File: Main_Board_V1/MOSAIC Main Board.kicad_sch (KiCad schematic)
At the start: 82 parts, among them J1 CONN E, J10 Right Angle Qwiic Connector, J11 Vertical Qwiic Connector, J12 CONN E, J13 CONN E, J14 35RAPC4BH3 CONN 3.5MM, J2 CONN E, J3 CONN E, J4 CONN HEADER VERT 10POS 1.27MM, J5 USB TYPE C R/A SMT 16PIN, J9 BATT JST-2-SMD, Q1 MOSFET P-CH 30V 3.1A SOT23-3, U1 IC SWITCH SP3T X 2 750mOhm TD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, U2 TVS DIODE 3.3VWM 6VC SOT26, U3 MCP73831 IC BATT CNTL, U4 IC REG LINEAR 3.3V 1A 8UDFN, U5 AP7347DQ-33W5-7K-3.3V

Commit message: started JLCPCB setup
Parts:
- J1, J12, J13, J2, J3: FT Rotation Offset (none) -> 180
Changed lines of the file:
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@@
 			)
 		)
+		(property "FT Rotation Offset" "180"
+			(at 154.178 216.408 0)
+			(effects
+				(font
+					(size 1.27 1.27)
+				)
+				(hide yes)
+			)
+		)
 		(pin "19"
 		)
@@
 			)
 		)
+		(property "FT Rotation Offset" "180"
+			(at 301.244 210.693 0)
+			(effects
+				(font
+					(size 1.27 1.27)
+				)
+				(hide yes)
+			)
+		)
 		(pin "18"
 		)
@@
 			)
 		)
+		(property "FT Rotation Offset" "180"
+			(at 62.738 216.408 0)
+			(effects
+				(font
+					(size 1.27 1.27)
+				)
+				(hide yes)
+			)
+		)
 		(pin "1"
 		)
@@
 			)
 		)
+		(property "FT Rotation Offset" "180"
+			(at 234.823 210.439 0)
+			(effects
+				(font
+					(size 1.27 1.27)
+				)
+				(hide yes)
+			)
+		)
 		(pin "18"
 		)
@@
 			(at 93.218 97.028 0)
 			(effects
+				(font
+					(size 1.27 1.27)
+				)
+				(hide yes)
+			)
+		)
+		(property "FT Rotation Offset" "180"
+			(at 93.218 97.028 0)
+			(effects

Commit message: Finished JLCPCB setup
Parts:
- C3: JLCPCB Part # C18212337 -> C20617880
- D1, D2, D3, D4, D5, S1, S2, S3, U2: FT Rotation Offset (none) -> 180
- J10: JLCPCB Part # C145956 -> C7527619
- Q1, U1, U5: FT Rotation Offset (none) -> -90
- renumbered SWDIO2 to SWDIO1
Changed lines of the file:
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@@
 			)
 		)
+		(property "FT Rotation Offset" "180"
+			(at 243.078 134.874 90)
+			(effects
+				(font
+					(size 1.27 1.27)
+				)
+				(hide yes)
+			)
+		)
 		(pin "A"
 		)
@@
 			)
 		)
+		(property "FT Rotation Offset" "-90"
+			(at 319.278 48.768 0)
+			(effects
+				(font
+					(size 1.27 1.27)
+				)
+				(hide yes)
+			)
+		)
 		(pin "3"
 		)
@@
 			)
 		)
+		(property "FT Rotation Offset" "-90"
+			(at 250.19 285.75 0)
+			(effects
+				(font
+					(size 1.27 1.27)
+				)
+				(hide yes)
+			)
+		)
 		(pin "2"
 		)
@@
 			)
 		)
+		(property "FT Rotation Offset" "180"
+			(at 278.638 69.088 0)
+			(effects
+				(font
+					(size 1.27 1.27)
+				)
+				(hide yes)
+			)
+		)
 		(pin "1"
 		)
@@
 			)
 		)
+		(property "FT Rotation Offset" "180"
+			(at 227.838 135.128 90)
+			(effects
+				(font
+					(size 1.27 1.27)
+				)
+				(hide yes)
+			)
+		)
 		(pin "A"
 		)
@@
 		(on_board yes)
 		(dnp no)
-		(property "Reference" "SWDIO2"
+		(property "Reference" "SWDIO1"
 			(at 276.0206 154.5376 0)
 			(effects
@@
 			(project "MOSAIC Main Board"
 				(path "/52f21295-3640-410f-ad83-534235adfded"
-					(reference "SWDIO2")
+					(reference "SWDIO1")
 					(unit 1)
 				)
@@
 			)
 		)
-		(property "Datasheet" "https://www.digikey.com/en/products/detail/kemet/C0603C104J4RAC7867/411096"
+		(property "Datasheet" "https://jlcpcb.com/api/file/downloadByFileSystemAccessId/8590922676573577216"
 			(at 352.298 69.088 0)
 			(effects
@@
 			)
 		)
-		(property "Description" "https://jlcpcb.com/partdetail/-KAF21BR71H104JT/C18212337"
+		(property "Description" "https://jlcpcb.com/partdetail/21992639-0805CG0R1C500NT/C20617880"
 			(at 352.298 69.088 0)
 			(effects
@@
 			)
 		)
-		(property "JLCPCB Part #" "C18212337"
+		(property "JLCPCB Part #" "C20617880"
 			(at 352.298 69.088 0)
 			(effects
@@
 			)
 		)
+		(property "FT Rotation Offset" "180"
+			(at 171.958 130.048 0)
+			(effects
+				(font
+					(size 1.27 1.27)
+				)
+				(hide yes)
+			)
+		)
 		(pin "3"
 		)
@@
 			)
 		)
+		(property "FT Rotation Offset" "180"
+			(at 311.658 61.468 0)
+			(effects
+				(font
+					(size 1.27 1.27)
+				)
+				(hide yes)
+			)
+		)
 		(pin "C"
 		)
@@
 			)
 		)
+		(property "FT Rotation Offset" "-90"
+			(at 423.418 132.588 0)
+			(effects
+				(font
+					(size 1.27 1.27)
+				)
+				(hide yes)
+			)
+		)
 		(pin "3"
 		)
@@
 			)
 		)
+		(property "FT Rotation Offset" "180"
+			(at 212.598 135.128 90)
+			(effects
+				(font
+					(size 1.27 1.27)
+				)
+				(hide yes)
+			)
+		)
 		(pin "A"
 		)
@@
 			)
 		)
+		(property "FT Rotation Offset" "180"
+			(at 311.658 140.208 90)
+			(effects
+				(font
+					(size 1.27 1.27)
+				)
+				(hide yes)
+			)
+		)
 		(pin "A"
 		)
@@
 			)
 		)
+		(property "FT Rotation Offset" "180"
+			(at 169.418 117.348 0)
+			(effects
+				(font
+					(size 1.27 1.27)
+				)
+				(hide yes)
+			)
+		)
 		(pin "3"
 		)
@@
 		)
 		(property "Value" "Right Angle Qwiic Connector"
-			(at 350.266 170.688 0)
+			(at 369.443 191.262 0)
 			(effects
 				(font
@@
 				)
 				(justify left top)
+				(hide yes)
 			)
 		)
@@
 			)
 		)
-		(property "Datasheet" "https://jlcpcb.com/api/file/downloadByFileSystemAccessId/8588895674171052032"
+		(property "Datasheet" "https://jlcpcb.com/api/file/downloadByFileSystemAccessId/8590907288981364736"
 			(at 374.523 185.928 0)
 			(effects
@@
 			)
 		)
-		(property "Description" "https://jlcpcb.com/partdetail/C145956"
+		(property "Description" "https://jlcpcb.com/partdetail/Lian_XinTechnology-XDWF_091004P/C7527619"
 			(at 374.523 185.928 0)
 			(effects
@@
 			)
 		)
-		(property "JLCPCB Part #" "C145956"
+		(property "JLCPCB Part #" "C7527619"
 			(at 374.523 185.928 0)
 			(effects
@@
 			(at 169.418 107.188 0)
 			(effects
+				(font
+					(size 1.27 1.27)
+				)
+				(hide yes)
+			)
+		)
+		(property "FT Rotation Offset" "180"
+			(at 169.418 107.188 0)
+			(effects

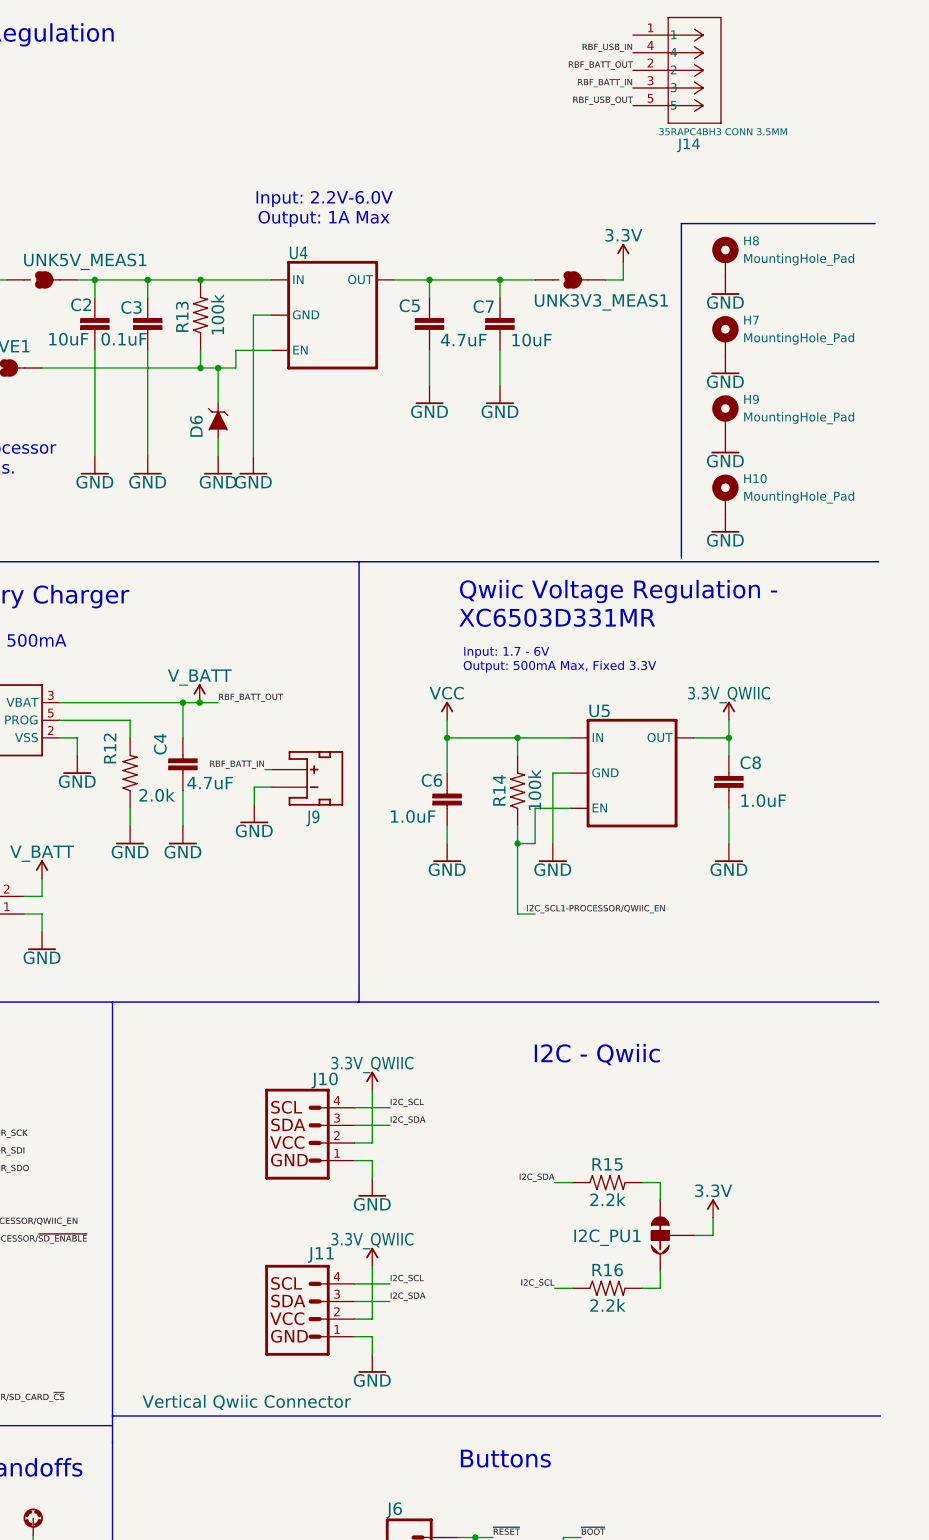
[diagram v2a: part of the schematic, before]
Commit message: added bom
Added bom for assembly after JLCPCB assembly.
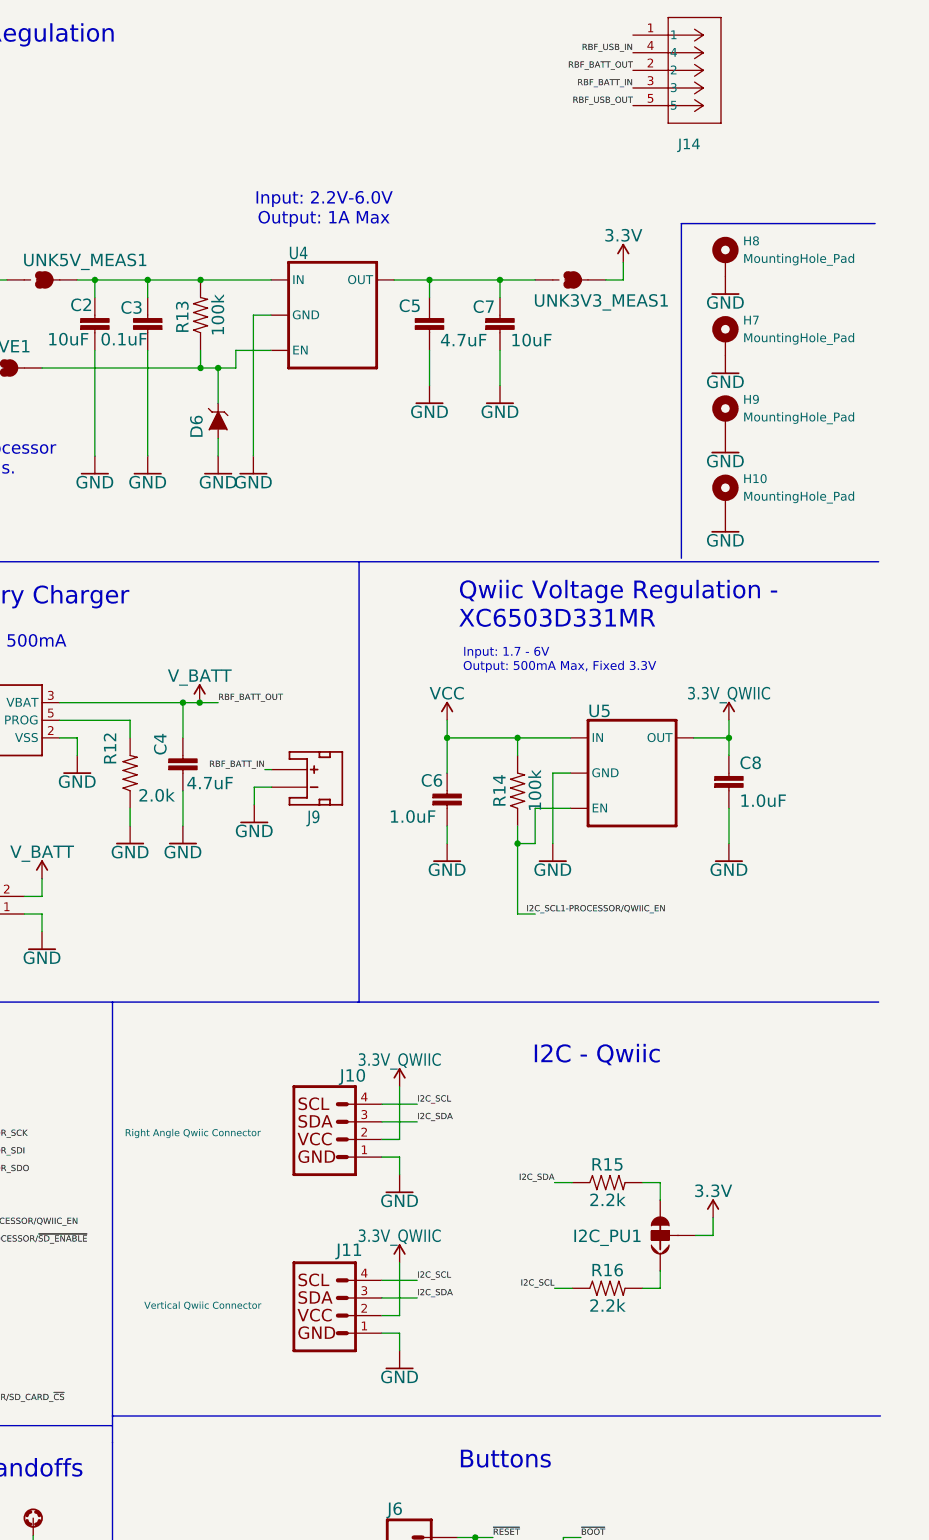
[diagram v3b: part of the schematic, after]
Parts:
- C1, C2, C3, C4, C5, C6, C7, C8, D1, D2, D3, D4, D5, D6, F1, J1, J10, J11, J12, J13, J2, J3, J5, LOGO1, LOGO2, Q1, R1, R10, R11, R12, R13, R14, R15, R16, R2, R3, R4, R5, R6, R7, R8, R9, S1, S2, S3, S4, S5, U1, U2, U3, U4, U5: now left out of the parts list
- H3: Source https://www.digikey.com/en/products/detail/w%C3%BCrth-elekt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 -> (none); now in the parts list
- J14: Source https://www.mouser.com/ProductDetail/Switchcraft/35RAPC4BH3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 -> (none); now in the parts list
- J9: value BATT JST-2-SMD -> CONN_JST_BATT; now in the parts list
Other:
- moved on the sheet: J10, J11

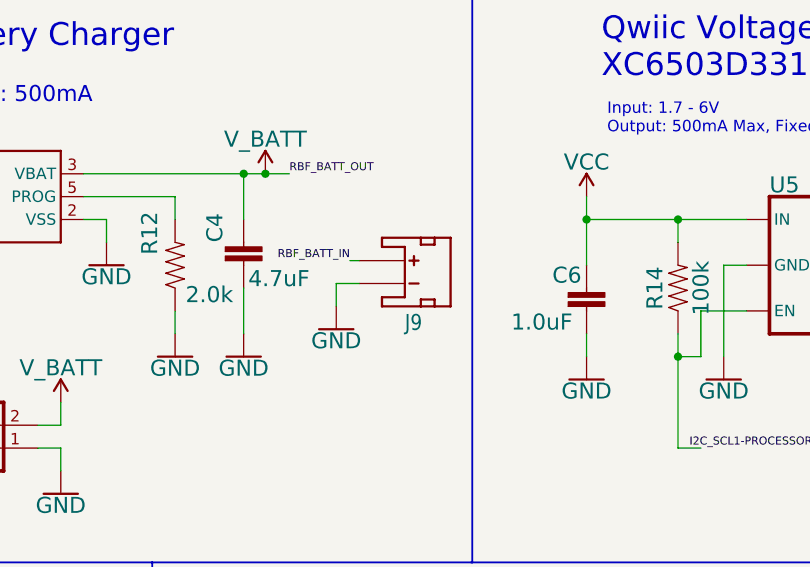
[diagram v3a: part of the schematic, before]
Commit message: fixed jlcpcb comp placement
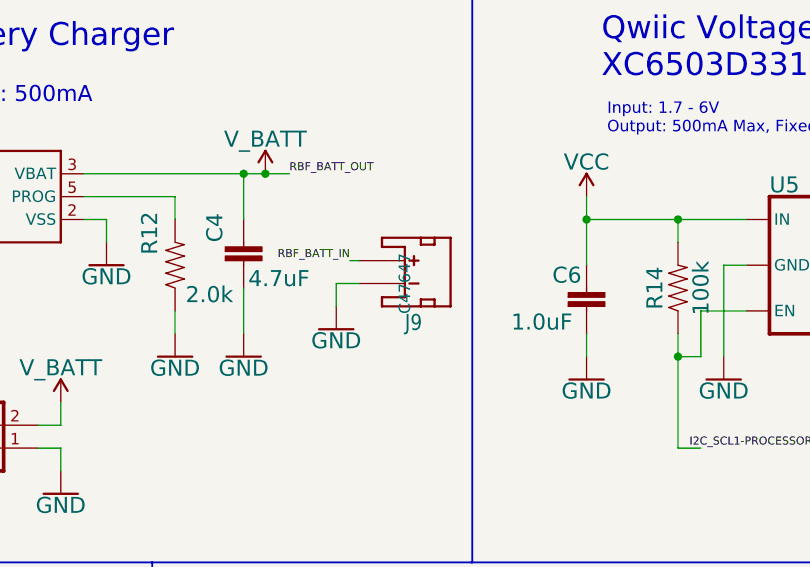
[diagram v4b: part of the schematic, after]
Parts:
- C1, C2, C3, C4, C5, C6, C7, C8, D1, D2, D3, D4, D5, D6, F1, J1, J10, J11, J12, J13, J2, J3, J5, Q1, R1, R10, R11, R12, R13, R14, R15, R16, R2, R3, R4, R5, R6, R7, R8, R9, S1, S2, S3, S4, S5, U1, U2, U3, U4, U5: now in the parts list
- H1, H2, H3, H4, H5, H6: now left out of the parts list
- J14: footprint main_board_footprints_V1.0:CONN_35RAPC4BH3_SWC -> CONN_35RAPC4BH3_SWC; now left out of the parts list
- J9: JLCPCB Part # (none) -> C47647
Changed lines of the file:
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@@
 			)
 		)
-		(property "Datasheet" "https://www.sparkfun.com/datasheets/Prototyping/Connectors/JST-Horizontal.pdf"
+		(property "Datasheet" "https://jlcpcb.com/api/file/downloadByFileSystemAccessId/8588893957006757888"
 			(at 375.285 134.62 0)
 			(effects
@@
 			)
 		)
-		(property "Description" "https://www.mouser.com/ProductDetail/485-1769"
+		(property "Description" "https://jlcpcb.com/partdetail/48652-PH_2PSurface_Mount_RightAngle/C47647"
 			(at 375.285 134.62 0)
 			(effects
@@
 			)
 		)
+		(property "JLCPCB Part #" "C47647"
+			(at 375.285 134.62 0)
+			(effects
+				(font
+					(size 1.27 1.27)
+				)
+			)
+		)
 		(pin "1"
 		)
@@
 		(unit 1)
 		(exclude_from_sim no)
-		(in_bom no)
+		(in_bom yes)
 		(on_board yes)
 		(dnp no)
@@
 		(unit 1)
 		(exclude_from_sim no)
-		(in_bom yes)
+		(in_bom no)
 		(on_board yes)
 		(dnp no)
@@
 			)
 		)
-		(property "Footprint" "main_board_footprints_V1.0:CONN_35RAPC4BH3_SWC"
+		(property "Footprint" "CONN_35RAPC4BH3_SWC"
 			(at 424.434 40.513 0)
 			(effects
@@
 			)
 		)
-		(property "Description" "https://www.mouser.com/ProductDetail/Switchcraft/35RAPC4BH3?qs=I3kMT7EEIOWFGyk5rynRAQ%3D%3D"
+		(property "Description" "https://www.digikey.com/en/products/detail/switchcraft-inc/35RAPC4BH3/1288781?s=N4IgTCBcDaIMwFYBKBBACgYQCwCEAScIAugL5A"
 			(at 422.275 26.162 0)
 			(effects
@@
 		(unit 1)
 		(exclude_from_sim no)
-		(in_bom no)
+		(in_bom yes)
 		(on_board yes)
 		(dnp no)
@@
 		(unit 1)
 		(exclude_from_sim no)
-		(in_bom no)
+		(in_bom yes)
 		(on_board yes)
 		(dnp no)
@@
 		(unit 1)
 		(exclude_from_sim no)
-		(in_bom no)
+		(in_bom yes)
 		(on_board yes)
 		(dnp no)
@@
 		(unit 1)
 		(exclude_from_sim no)
-		(in_bom no)
+		(in_bom yes)
 		(on_board yes)
 		(dnp no)
@@
 		(unit 1)
 		(exclude_from_sim no)
-		(in_bom no)
+		(in_bom yes)
 		(on_board yes)
 		(dnp no)
@@
 		(unit 1)
 		(exclude_from_sim no)
-		(in_bom no)
+		(in_bom yes)
 		(on_board yes)
 		(dnp no)
@@
 		(unit 1)
 		(exclude_from_sim no)
-		(in_bom no)
+		(in_bom yes)
 		(on_board yes)
 		(dnp no)
@@
 		(unit 1)
 		(exclude_from_sim no)
-		(in_bom yes)
+		(in_bom no)
 		(on_board yes)
 		(dnp no)
@@
 		(unit 1)
 		(exclude_from_sim no)
-		(in_bom no)
+		(in_bom yes)
 		(on_board yes)
 		(dnp no)
@@
 		(unit 1)
 		(exclude_from_sim no)
-		(in_bom no)
+		(in_bom yes)
 		(on_board yes)
 		(dnp no)
@@
 		(unit 1)
 		(exclude_from_sim no)
-		(in_bom no)
+		(in_bom yes)
 		(on_board yes)
 		(dnp no)
@@
 		(unit 1)
 		(exclude_from_sim no)
-		(in_bom no)
+		(in_bom yes)
 		(on_board yes)
 		(dnp no)
@@
 		(unit 1)
 		(exclude_from_sim no)
-		(in_bom no)
+		(in_bom yes)
 		(on_board yes)
 		(dnp no)
@@
 		(unit 1)
 		(exclude_from_sim no)
-		(in_bom no)
+		(in_bom yes)
 		(on_board yes)
 		(dnp no)
@@
 		(unit 1)
 		(exclude_from_sim no)
-		(in_bom no)
+		(in_bom yes)
 		(on_board yes)
 		(dnp no)
@@
 		(unit 1)
 		(exclude_from_sim no)
-		(in_bom no)
+		(in_bom yes)
 		(on_board yes)
 		(dnp no)
@@
 		(unit 1)
 		(exclude_from_sim no)
-		(in_bom no)
+		(in_bom yes)
 		(on_board yes)
 		(dnp no)
@@
 		(unit 1)
 		(exclude_from_sim no)
-		(in_bom yes)
+		(in_bom no)
 		(on_board yes)
 		(dnp no)
@@
 		(unit 1)
 		(exclude_from_sim no)
-		(in_bom no)
+		(in_bom yes)
 		(on_board yes)
 		(dnp no)
@@
 		(unit 1)
 		(exclude_from_sim no)
-		(in_bom no)
+		(in_bom yes)
 		(on_board yes)
 		(dnp no)
@@
 		(unit 1)
 		(exclude_from_sim no)
-		(in_bom no)
+		(in_bom yes)
 		(on_board yes)
 		(dnp no)
@@
 		(unit 1)
 		(exclude_from_sim no)
-		(in_bom no)
+		(in_bom yes)
 		(on_board yes)
 		(dnp no)
@@
 		(unit 1)
 		(exclude_from_sim no)
-		(in_bom no)
+		(in_bom yes)
 		(on_board yes)
 		(dnp no)
@@
 		(unit 1)
 		(exclude_from_sim no)
-		(in_bom no)
+		(in_bom yes)
 		(on_board yes)
 		(dnp no)
@@
 		(unit 1)
 		(exclude_from_sim no)
-		(in_bom yes)
+		(in_bom no)
 		(on_board yes)
 		(dnp no)
@@
 		(unit 1)
 		(exclude_from_sim no)
-		(in_bom no)
+		(in_bom yes)
 		(on_board yes)
 		(dnp no)
@@
 		(unit 1)
 		(exclude_from_sim no)
-		(in_bom no)
+		(in_bom yes)
 		(on_board yes)
 		(dnp no)
@@
 		(unit 1)
 		(exclude_from_sim no)
-		(in_bom no)
+		(in_bom yes)
 		(on_board yes)
 		(dnp no)
@@
 		(unit 1)
 		(exclude_from_sim no)
-		(in_bom no)
+		(in_bom yes)
 		(on_board yes)
 		(dnp no)
@@
 		(unit 1)
 		(exclude_from_sim no)
-		(in_bom yes)
+		(in_bom no)
 		(on_board yes)
 		(dnp no)
@@
 		(unit 1)
 		(exclude_from_sim no)
-		(in_bom no)
+		(in_bom yes)
 		(on_board yes)
 		(dnp no)
@@
 		(unit 1)
 		(exclude_from_sim no)
-		(in_bom no)
+		(in_bom yes)
 		(on_board yes)
 		(dnp no)
@@
 		(unit 1)
 		(exclude_from_sim no)
-		(in_bom yes)
+		(in_bom no)
 		(on_board yes)
 		(dnp no)
@@
 		(unit 1)
 		(exclude_from_sim no)
-		(in_bom no)
+		(in_bom yes)
 		(on_board yes)
 		(dnp no)
@@
 		(unit 1)
 		(exclude_from_sim no)
-		(in_bom yes)
+		(in_bom no)
 		(on_board yes)
 		(dnp no)
@@
 		(unit 1)
 		(exclude_from_sim no)
-		(in_bom no)
+		(in_bom yes)
 		(on_board yes)
 		(dnp no)
@@
 		(unit 1)
 		(exclude_from_sim no)
-		(in_bom no)
+		(in_bom yes)
 		(on_board yes)
 		(dnp no)
@@
 		(unit 1)
 		(exclude_from_sim no)
-		(in_bom no)
+		(in_bom yes)
 		(on_board yes)
 		(dnp no)
@@
 		(unit 1)
 		(exclude_from_sim no)
-		(in_bom no)
+		(in_bom yes)
 		(on_board yes)
 		(dnp no)
@@
 		(unit 1)
 		(exclude_from_sim no)
-		(in_bom no)
+		(in_bom yes)
 		(on_board yes)
 		(dnp no)
@@
 		(unit 1)
 		(exclude_from_sim no)
-		(in_bom no)
+		(in_bom yes)
 		(on_board yes)
 		(dnp no)
@@
 		(unit 1)
 		(exclude_from_sim no)
-		(in_bom no)
+		(in_bom yes)
 		(on_board yes)
 		(dnp no)
@@
 		(unit 1)
 		(exclude_from_sim no)
-		(in_bom no)
+		(in_bom yes)
 		(on_board yes)
 		(dnp no)
@@
 		(unit 1)
 		(exclude_from_sim no)
-		(in_bom no)
+		(in_bom yes)
 		(on_board yes)
 		(dnp no)
@@
 		(unit 1)
 		(exclude_from_sim no)
-		(in_bom no)
+		(in_bom yes)
 		(on_board yes)
 		(dnp no)
@@
 		(unit 1)
 		(exclude_from_sim no)
-		(in_bom no)
+		(in_bom yes)
 		(on_board yes)
 		(dnp no)
@@
 		(unit 1)
 		(exclude_from_sim no)
-		(in_bom no)
+		(in_bom yes)
 		(on_board yes)
 		(dnp no)
@@
 		(unit 1)
 		(exclude_from_sim no)
-		(in_bom no)
+		(in_bom yes)
 		(on_board yes)
 		(dnp no)
@@
 		(unit 1)
 		(exclude_from_sim no)
-		(in_bom no)
+		(in_bom yes)
 		(on_board yes)
 		(dnp no)
@@
 		(unit 1)
 		(exclude_from_sim no)
-		(in_bom no)
+		(in_bom yes)
 		(on_board yes)
 		(dnp no)
@@
 		(unit 1)
 		(exclude_from_sim no)
-		(in_bom no)
+		(in_bom yes)
 		(on_board yes)
 		(dnp no)
@@
 		(unit 1)
 		(exclude_from_sim no)
-		(in_bom no)
+		(in_bom yes)
 		(on_board yes)
 		(dnp no)
@@
 		(unit 1)
 		(exclude_from_sim no)
-		(in_bom no)
+		(in_bom yes)
 		(on_board yes)
 		(dnp no)
@@
 		(unit 1)
 		(exclude_from_sim no)
-		(in_bom no)
+		(in_bom yes)
 		(on_board yes)
 		(dnp no)
@@
 		(unit 1)
 		(exclude_from_sim no)
-		(in_bom no)
+		(in_bom yes)
 		(on_board yes)
 		(dnp no)

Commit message: minor changes to text sizing
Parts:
- U5: value AP7347DQ-33W5-7K-3.3V -> XC6503D331MR-500mA-3.3V; symbol main_board_symbols_V1.0:AP7347DQ-33W5-7K-3.3V -> main_board_symbols_V1.0:XC6503D331MR-500mA-3.3V
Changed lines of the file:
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@@
 	)
 	(symbol
-		(lib_id "main_board_symbols_V1.0:AP7347DQ-33W5-7K-3.3V")
+		(lib_id "main_board_symbols_V1.0:XC6503D331MR-500mA-3.3V")
 		(at 423.418 132.588 0)
 		(unit 1)
@@
 			)
 		)
-		(property "Value" "AP7347DQ-33W5-7K-3.3V"
-			(at 407.924 148.59 0)
+		(property "Value" "XC6503D331MR-500mA-3.3V"
+			(at 415.798 140.462 0)
 			(effects
 				(font
